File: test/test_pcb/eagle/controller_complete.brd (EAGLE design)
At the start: 50.8 x 33 mm, 57 parts, among them Q1 MOSFET-N, Q2 P-MOSFET, Q4 P-MOSFET, U1 XC6504-LINEAR-REGULATOR, U2 PIC24FJ64GA306, U4 RN4020_BT_4.0_MODULE, U5 FLASH8MSOP8

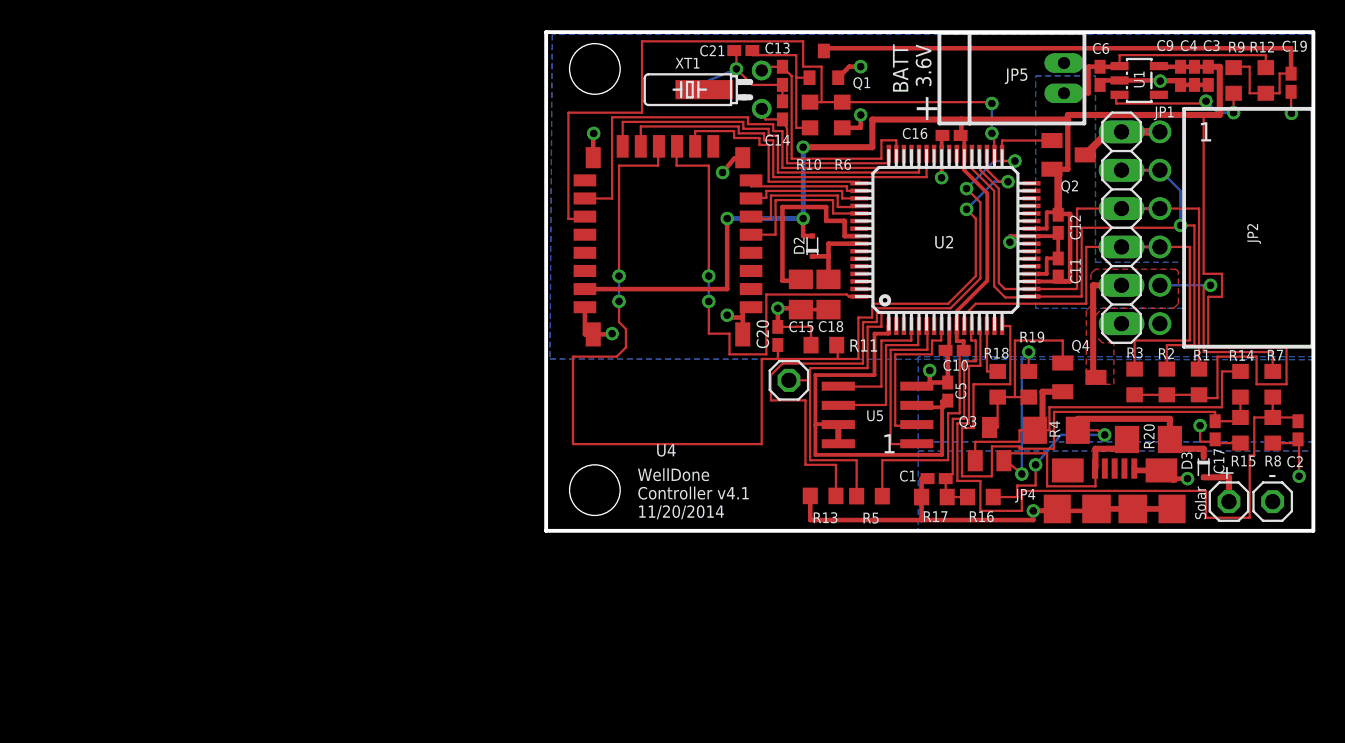
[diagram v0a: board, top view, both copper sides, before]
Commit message: Split pymomo into iotilecore and iotilebuild repositories (#6)
* Add copyright origin headers to all files

* Rename pymomo to iotilecore and remove old test files

* Finish renaming pymomo to iotile

* update remaining files with name change

* Rename momo tool and remove outdated tools

* Update to fix compilation issues, remove ultrasound

* Update config settings path

* Remove outdated test scripts

* Remove unintentional test code

* Update test cases to use new part cache since pickled names changed

* Initial split of build system out of iotilecore

* Fix external proxy module support after pymomo name change
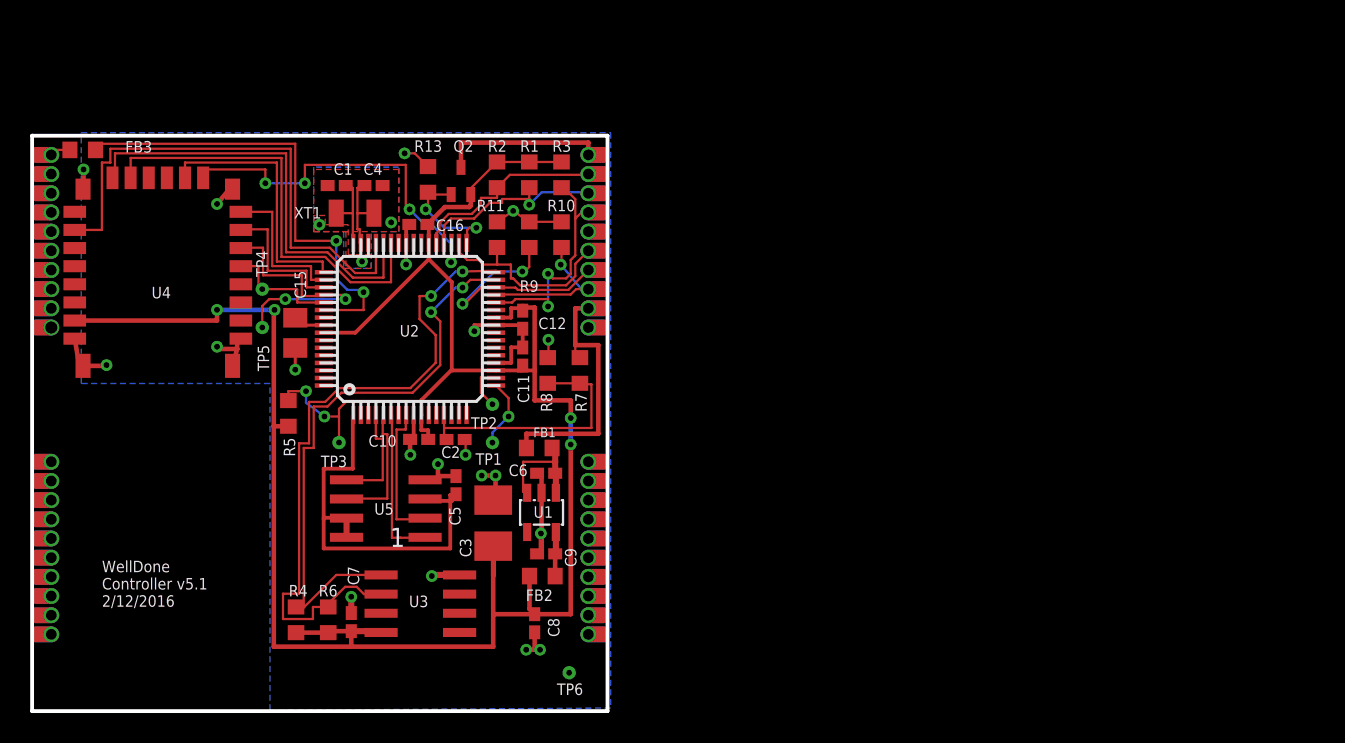
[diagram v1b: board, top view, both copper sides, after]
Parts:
- removed C13, C14: 18 pF, rcl:C0402K
- removed C17: 100 nF, rcl:C0402K
- removed C18: 10 uF, rcl:C0805K
- removed C19, C21: 1 uF, rcl:C0402K
- removed C20: 22 pF, rcl:C0402K
- removed D2, D3: (no value), diode:SC79_INFINEON
- removed JP1: MOMO-VERT-6M, components:1X06
- removed JP2: MOMO-EDGE-6F, components:MOMO-EDGE-8F
- removed JP3, JP7, JP8: (no value), pinhead:1X01
- removed JP4: CONN-MICROUSB-B-RCPT, custom_ics:MICROUSB-B-FCI
- removed JP5: MOMO-PWR-HOUSED, components:MOMO-PWR-HOUSED
- removed Q1: MOSFET-N, custom_ics:SOT-23
- removed Q3: (no value), transistor-pnp:SOT23
- removed Q4: P-MOSFET, components:SOT23
- removed R12, R14, R15, R16, R17: 510K, rcl:R0603
- removed R18: 10K, rcl:R0603
- removed R19: 100K, rcl:R0603
- removed R20: 1 ohm, rcl:R1206
- added C7: 100nF, rcl:C0402K
- added C8: 10 pF, rcl:C0402K
- added FB1, FB2, FB3: (no value), rcl:R0603
- added MOD1: M22_MODULE, formfactors:M22_MODULE
- added TP1, TP2, TP3, TP4, TP5, TP6: TESTPAD-15MIL, connectors:TESTPAD-15MIL
- added U3: ATECC508A, custom_ics:SOIC8
- C1: value 100 nF -> 22 pF
- C3: value 33 pF -> 100 uF; device rcl:C0402K -> rcl:B/3528-21R
- C4: value 10 pF -> 22 pF
- Q2: value P-MOSFET -> P-MOSFET-SC70; device components:SOT23 -> components:SOT323-BEC
- R1, R2, R3: value 10K -> 1K
- R10, R11: value 100K -> 10K
- R4: value 1 ohm -> 1K; device rcl:R1206 -> rcl:R0603
- R6: value 100K -> 1K
- XT1: value 32.768khz -> 32.768 khz; device components:TC26H -> components:2-SMD-XTAL
- moved C3 55.8 mm to (30.5, 12.4)
- moved C2 55.8 mm to (28.0, 18.0), turned to 0 degrees
- moved C4 54.8 mm to (22.6, 34.8), turned to 0 degrees
- moved C9 52.6 mm to (34.0, 10.4), turned to 180 degrees
- moved R4 51.9 mm to (17.5, 6.05), turned to 270 degrees
- moved U1 48.8 mm to (33.7, 13.2), turned to 180 degrees
- moved R8 48.2 mm to (34.1, 22.6), turned to 270 degrees
- moved R9 47.7 mm to (32.9, 31.5), turned to 270 degrees
- moved R6 47.7 mm to (19.6, 6.05), turned to 270 degrees
- moved R1 46.4 mm to (32.9, 35.5), turned to 90 degrees
- moved R2 46.4 mm to (30.8, 35.5), turned to 90 degrees
- moved R7 45.9 mm to (36.3, 22.6)
- moved C6 45.1 mm to (34.0, 15.7), turned to 180 degrees
- moved C1 44.2 mm to (20.2, 34.8)
- moved R3 40.4 mm to (35.1, 35.5), turned to 90 degrees
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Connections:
- removed net CHG_I+: D3.C, R16.2, R20.2, R4.1
- removed net CHG_I-: Q3.1, Q4.2, R14.2, R4.2
- removed net HW_RESET: R10.2, R6.2, U2.34, U4.PIO7
- removed net N$10: Q3.3, Q4.1, R18.2, R19.1
- removed net N$11: C19.1, Q1.3, R12.1, R9.2
- removed net PIO3: U2.64, U4.PIO3
- removed net PIO4: C20.1, R11.2, U2.35, U4.PIO4
- removed net SAMP_CHG+: C1.1, R16.1, R17.2, U2.12
- removed net SAMP_CHG-: C17.1, R14.1, R15.2, U2.16
- removed net VBAT: C18.1, D2.C, U2.57
- new net HSCLK: MOD1.IOTILEA_6, R11.2, U2.34
- new net HSDIN: MOD1.IOTILEA_7, R9.2, U2.30
- new net HSDOUT: MOD1.IOTILEA_8, R10.2, U2.29
- new net N$8: FB3.2, MOD1.IOA_1
- new net SCL2: R6.1, U2.32, U3.6
- new net SDA2: R4.1, U2.31, U3.5
- net CHG_EN: now also FB3.1, U2.54; no longer R18.1, U2.14
- net CONN: now also U2.35
- net GND: now also C3.-, C7.2, C8.2, MOD1.IOTILEA_10, R10.1, R9.1, TP6.P$1, U3.4; no longer C13.2, C14.2, C17.2, C18.2, C19.2, C20.2, C21.2, C3.2, JP1.7, JP2.GND, JP4.5, JP4.GND2, JP4.GND3, JP4.GND4, JP4.GND5, JP4.GND6, JP5.2, JP7.1, Q1.2, R15.1, R17.1, R6.1
- net ICLK: now also MOD1.IOTILEA_2; no longer JP1.3, JP2.CLK, U2.17
- net IDAT: now also MOD1.IOTILEA_3; no longer JP1.4, JP2.DAT, U2.18
- net IRQ: now also MOD1.IOTILEA_4, U2.28; no longer JP1.5, JP2.ARLM, U2.11
- net N$1: now also C9.1, FB2.1, U1.5; no longer R9.1, U1.3
- net N$2: now also C6.1, FB1.2, U1.1, U1.3; no longer C21.1, Q1.1, R10.1
- net N$3: now also C1.1, U2.48, XT1.1; no longer D3.A, JP8.1
- net N$4: now also TP3.P$1; no longer JP3.1
- net N$5: now also C4.1, U2.47, XT1.2; no longer JP4.1, Q3.2, R19.2, R20.1
- net N$6: now also TP1.P$1, U2.17; no longer C14.1, U2.47, XT1.2
- net N$7: now also TP2.P$1, U2.18; no longer C13.1, U2.48, XT1.1
- net RX: now also TP5.P$1
- net TX: now also TP4.P$1
- net V+: now also FB1.1, MOD1.IOTILEA_9; no longer C6.1, JP1.6, JP2.V4, JP5.1, Q4.3, R12.2, U1.1
- net VCCINT: now also C3.+, C7.1, C8.1, FB2.2, R4.2, R6.2, U2.57, U3.8; no longer C3.1, C4.1, C9.1, D2.A, U1.5
- net VCCIO: now also MOD1.IOTILEA_1; no longer JP1.1, JP2.V28
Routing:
- net PIO4: track 75.2 -> 0.00 mm, vias 4 -> 0
- net GND: track 105.0 -> 55.3 mm, vias 17 -> 23
- net HW_RESET: track 49.3 -> 0.00 mm, vias 2 -> 0
- net SCL2: track 0.00 -> 44.4 mm, vias 0 -> 2
- net N$11: track 39.8 -> 0.00 mm
- net SDA2: track 0.00 -> 39.5 mm, vias 0 -> 2
- net SAMP_CHG-: track 38.9 -> 0.00 mm
- net VCC_EN: track 46.9 -> 8.96 mm
- net ICLK: track 45.7 -> 13.3 mm, vias 1 -> 0
- net VBAT_SAMP: track 47.9 -> 17.5 mm
- net PIO3: track 29.9 -> 0.00 mm, vias 2 -> 0
- net CHG_I-: track 27.4 -> 0.00 mm
- net CHG_EN: track 4.01 -> 31.3 mm, vias 0 -> 2
- net CONN: track 0.00 -> 26.2 mm, vias 0 -> 4
- net IDAT: track 38.5 -> 13.5 mm, vias 0 -> 1
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- added copper zone on layer 1, net GND
- removed copper zone on layer 1, net V+
- removed copper zone on layer 16, net V+
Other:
- board size 50.8 x 33 mm -> 38.1 x 38.1 mm
- board text added: "WellDone Controller v5.1 2/12/2016"
- board text removed: "+"
- board text removed: "-"
- board text removed: "BATT 3.6V"
- board text removed: "Solar"
- board text removed: "WellDone Controller v4.1 11/20/2014"
